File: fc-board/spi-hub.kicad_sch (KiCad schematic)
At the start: 22 parts, among them J15 BCS-110-L-D-TE, U10 LTC2983ILX-PBF

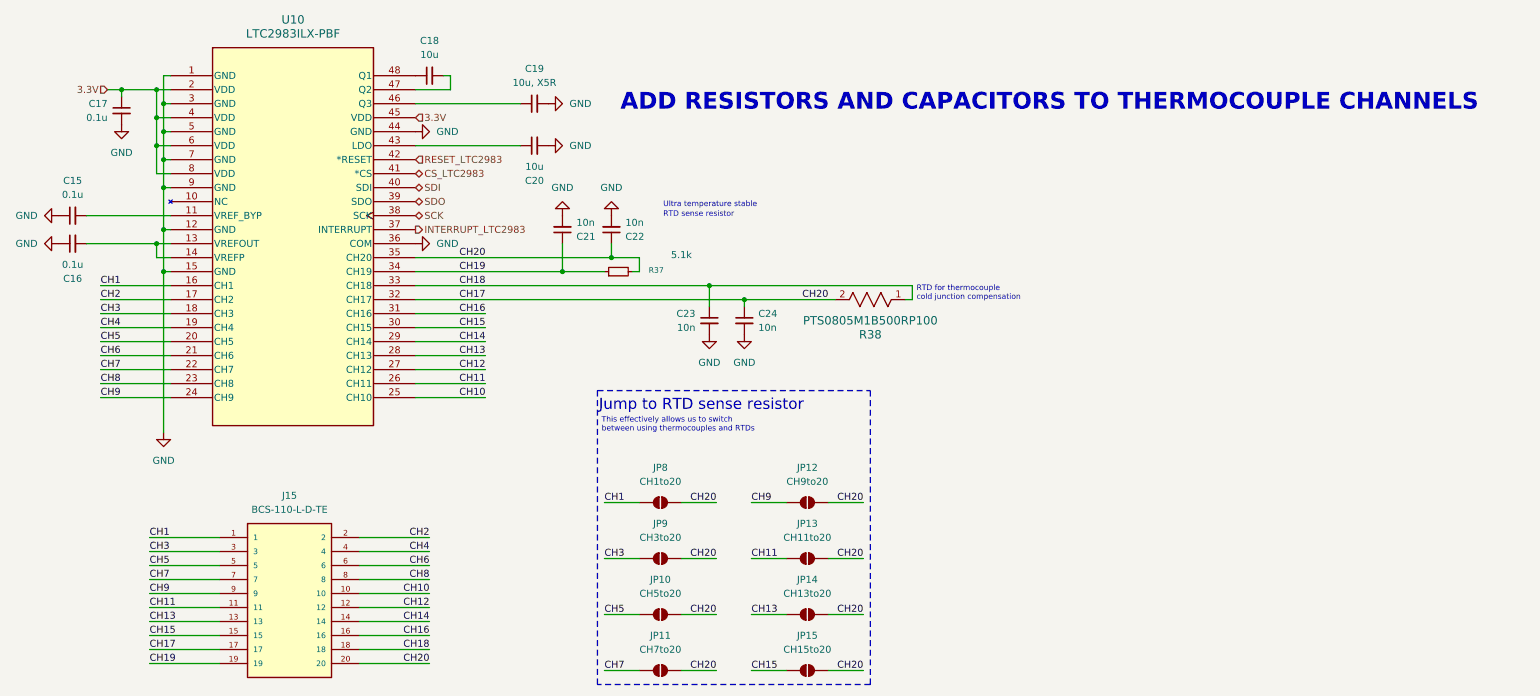
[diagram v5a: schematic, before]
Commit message: Fixed incorrect routes, modified gondola eth, cosmetics
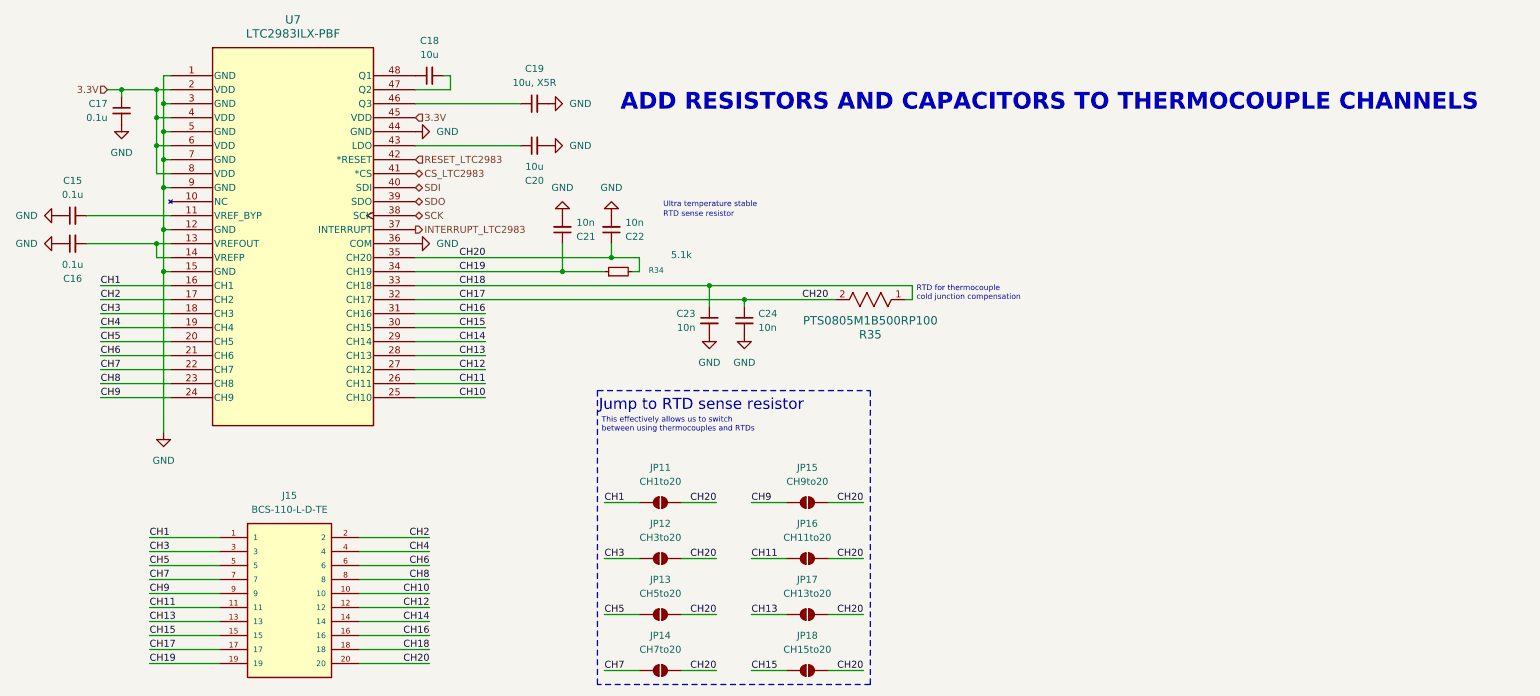
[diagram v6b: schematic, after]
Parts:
- renumbered JP8 to JP11, JP9 to JP12, JP10 to JP13, JP11 to JP14, JP12 to JP15, JP13 to JP16, JP14 to JP17, JP15 to JP18, R37 to R34, R38 to R35, U10 to U7
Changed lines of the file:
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@@
 	(title_block
 		(title "SPI Hub")
-		(date "2025-10-20")
+		(date "2025-12-08")
 		(rev "0.1")
 	)
@@
 		(dnp no)
 		(fields_autoplaced yes)
-		(property "Reference" "#PWR055"
+		(property "Reference" "#PWR052"
 			(at 43.18 100.33 0)
 			(effects
@@
 			(project "fc-board"
 				(path "/14bbabed-904f-4efc-8ba4-be00e59385c4/11d9cd03-29fa-40fa-a963-f5f11b91a482"
-					(reference "#PWR055")
+					(reference "#PWR052")
 					(unit 1)
 				)
@@
 		(dnp no)
 		(fields_autoplaced yes)
-		(property "Reference" "U10"
+		(property "Reference" "U7"
 			(at 66.675 19.05 0)
 			(effects
@@
 			(project ""
 				(path "/14bbabed-904f-4efc-8ba4-be00e59385c4/11d9cd03-29fa-40fa-a963-f5f11b91a482"
-					(reference "U10")
+					(reference "U7")
 					(unit 1)
 				)
@@
 		(dnp no)
 		(fields_autoplaced yes)
-		(property "Reference" "JP15"
+		(property "Reference" "JP18"
 			(at 160.02 130.81 0)
 			(effects
@@
 			(project ""
 				(path "/14bbabed-904f-4efc-8ba4-be00e59385c4/11d9cd03-29fa-40fa-a963-f5f11b91a482"
-					(reference "JP15")
+					(reference "JP18")
 					(unit 1)
 				)
@@
 		(dnp no)
 		(fields_autoplaced yes)
-		(property "Reference" "#PWR057"
+		(property "Reference" "#PWR054"
 			(at 95.25 59.69 0)
 			(effects
@@
 			(project "fc-board"
 				(path "/14bbabed-904f-4efc-8ba4-be00e59385c4/11d9cd03-29fa-40fa-a963-f5f11b91a482"
-					(reference "#PWR057")
+					(reference "#PWR054")
 					(unit 1)
 				)
@@
 		(dnp no)
 		(fields_autoplaced yes)
-		(property "Reference" "JP11"
+		(property "Reference" "JP14"
 			(at 133.35 130.81 0)
 			(effects
@@
 			(project "fc-board"
 				(path "/14bbabed-904f-4efc-8ba4-be00e59385c4/11d9cd03-29fa-40fa-a963-f5f11b91a482"
-					(reference "JP11")
+					(reference "JP14")
 					(unit 1)
 				)
@@
 		(dnp no)
 		(fields_autoplaced yes)
-		(property "Reference" "JP14"
+		(property "Reference" "JP17"
 			(at 160.02 120.65 0)
 			(effects
@@
 			(project "fc-board"
 				(path "/14bbabed-904f-4efc-8ba4-be00e59385c4/11d9cd03-29fa-40fa-a963-f5f11b91a482"
-					(reference "JP14")
+					(reference "JP17")
 					(unit 1)
 				)
@@
 		(on_board yes)
 		(dnp no)
-		(property "Reference" "R38"
+		(property "Reference" "R35"
 			(at 171.45 76.2 0)
 			(effects
@@
 			(project ""
 				(path "/14bbabed-904f-4efc-8ba4-be00e59385c4/11d9cd03-29fa-40fa-a963-f5f11b91a482"
-					(reference "R38")
+					(reference "R35")
 					(unit 1)
 				)
@@
 		(dnp no)
 		(fields_autoplaced yes)
-		(property "Reference" "JP13"
+		(property "Reference" "JP16"
 			(at 160.02 110.49 0)
 			(effects
@@
 			(project "fc-board"
 				(path "/14bbabed-904f-4efc-8ba4-be00e59385c4/11d9cd03-29fa-40fa-a963-f5f11b91a482"
-					(reference "JP13")
+					(reference "JP16")
 					(unit 1)
 				)
@@
 		(dnp no)
 		(fields_autoplaced yes)
-		(property "Reference" "JP9"
+		(property "Reference" "JP12"
 			(at 133.35 110.49 0)
 			(effects
@@
 			(project "fc-board"
 				(path "/14bbabed-904f-4efc-8ba4-be00e59385c4/11d9cd03-29fa-40fa-a963-f5f11b91a482"
-					(reference "JP9")
+					(reference "JP12")
 					(unit 1)
 				)
@@
 		(on_board yes)
 		(dnp no)
-		(property "Reference" "#PWR062"
+		(property "Reference" "#PWR059"
 			(at 142.24 82.55 0)
 			(effects
@@
 			(project "fc-board"
 				(path "/14bbabed-904f-4efc-8ba4-be00e59385c4/11d9cd03-29fa-40fa-a963-f5f11b91a482"
-					(reference "#PWR062")
+					(reference "#PWR059")
 					(unit 1)
 				)
@@
 		(dnp no)
 		(fields_autoplaced yes)
-		(property "Reference" "JP12"
+		(property "Reference" "JP15"
 			(at 160.02 100.33 0)
 			(effects
@@
 			(project "fc-board"
 				(path "/14bbabed-904f-4efc-8ba4-be00e59385c4/11d9cd03-29fa-40fa-a963-f5f11b91a482"
-					(reference "JP12")
+					(reference "JP15")
 					(unit 1)
 				)
@@
 		(dnp no)
 		(fields_autoplaced yes)
-		(property "Reference" "#PWR061"
+		(property "Reference" "#PWR058"
 			(at 124.46 48.26 0)
 			(effects
@@
 			(project "fc-board"
 				(path "/14bbabed-904f-4efc-8ba4-be00e59385c4/11d9cd03-29fa-40fa-a963-f5f11b91a482"
-					(reference "#PWR061")
+					(reference "#PWR058")
 					(unit 1)
 				)
@@
 		(dnp no)
 		(fields_autoplaced yes)
-		(property "Reference" "JP10"
+		(property "Reference" "JP13"
 			(at 133.35 120.65 0)
 			(effects
@@
 			(project "fc-board"
 				(path "/14bbabed-904f-4efc-8ba4-be00e59385c4/11d9cd03-29fa-40fa-a963-f5f11b91a482"
-					(reference "JP10")
+					(reference "JP13")
 					(unit 1)
 				)
@@
 		(dnp no)
 		(fields_autoplaced yes)
-		(property "Reference" "JP8"
+		(property "Reference" "JP11"
 			(at 133.35 100.33 0)
 			(effects
@@
 			(project "fc-board"
 				(path "/14bbabed-904f-4efc-8ba4-be00e59385c4/11d9cd03-29fa-40fa-a963-f5f11b91a482"
-					(reference "JP8")
+					(reference "JP11")
 					(unit 1)
 				)
@@
 		(on_board yes)
 		(dnp no)
-		(property "Reference" "#PWR063"
+		(property "Reference" "#PWR060"
 			(at 148.59 82.55 0)
 			(effects
@@
 			(project "fc-board"
 				(path "/14bbabed-904f-4efc-8ba4-be00e59385c4/11d9cd03-29fa-40fa-a963-f5f11b91a482"
-					(reference "#PWR063")
+					(reference "#PWR060")
 					(unit 1)
 				)
@@
 		(dnp no)
 		(fields_autoplaced yes)
-		(property "Reference" "#PWR054"
+		(property "Reference" "#PWR051"
 			(at 35.56 44.45 0)
 			(effects
@@
 			(project ""
 				(path "/14bbabed-904f-4efc-8ba4-be00e59385c4/11d9cd03-29fa-40fa-a963-f5f11b91a482"
-					(reference "#PWR054")
+					(reference "#PWR051")
 					(unit 1)
 				)
@@
 		(dnp no)
 		(fields_autoplaced yes)
-		(property "Reference" "#PWR056"
+		(property "Reference" "#PWR053"
 			(at 95.25 39.37 0)
 			(effects
@@
 			(project "fc-board"
 				(path "/14bbabed-904f-4efc-8ba4-be00e59385c4/11d9cd03-29fa-40fa-a963-f5f11b91a482"
-					(reference "#PWR056")
+					(reference "#PWR053")
 					(unit 1)
 				)
@@
 		(dnp no)
 		(fields_autoplaced yes)
-		(property "Reference" "#PWR052"
+		(property "Reference" "#PWR049"
 			(at 17.78 54.61 0)
 			(effects
@@
 			(project ""
 				(path "/14bbabed-904f-4efc-8ba4-be00e59385c4/11d9cd03-29fa-40fa-a963-f5f11b91a482"
-					(reference "#PWR052")
+					(reference "#PWR049")
 					(unit 1)
 				)
@@
 		(dnp no)
 		(fields_autoplaced yes)
-		(property "Reference" "#PWR058"
+		(property "Reference" "#PWR055"
 			(at 119.38 34.29 0)
 			(effects
@@
 			(project "fc-board"
 				(path "/14bbabed-904f-4efc-8ba4-be00e59385c4/11d9cd03-29fa-40fa-a963-f5f11b91a482"
-					(reference "#PWR058")
+					(reference "#PWR055")
 					(unit 1)
 				)
@@
 		(dnp no)
 		(fields_autoplaced yes)
-		(property "Reference" "#PWR053"
+		(property "Reference" "#PWR050"
 			(at 17.78 59.69 0)
 			(effects
@@
 			(project "fc-board"
 				(path "/14bbabed-904f-4efc-8ba4-be00e59385c4/11d9cd03-29fa-40fa-a963-f5f11b91a482"
-					(reference "#PWR053")
+					(reference "#PWR050")
 					(unit 1)
 				)
@@
 		(on_board yes)
 		(dnp no)
-		(property "Reference" "#PWR060"
+		(property "Reference" "#PWR057"
 			(at 115.57 48.26 0)
 			(effects
@@
 			(project "fc-board"
 				(path "/14bbabed-904f-4efc-8ba4-be00e59385c4/11d9cd03-29fa-40fa-a963-f5f11b91a482"
-					(reference "#PWR060")
+					(reference "#PWR057")
 					(unit 1)
 				)
@@
 		(dnp no)
 		(fields_autoplaced yes)
-		(property "Reference" "#PWR059"
+		(property "Reference" "#PWR056"
 			(at 119.38 41.91 0)
 			(effects
@@
 			(project "fc-board"
 				(path "/14bbabed-904f-4efc-8ba4-be00e59385c4/11d9cd03-29fa-40fa-a963-f5f11b91a482"
-					(reference "#PWR059")
+					(reference "#PWR056")
 					(unit 1)
 				)
@@
 		(on_board yes)
 		(dnp no)
-		(property "Reference" "R37"
+		(property "Reference" "R34"
 			(at 132.588 64.516 90)
 			(effects
@@
 			(project ""
 				(path "/14bbabed-904f-4efc-8ba4-be00e59385c4/11d9cd03-29fa-40fa-a963-f5f11b91a482"
-					(reference "R37")
+					(reference "R34")
 					(unit 1)
 				)

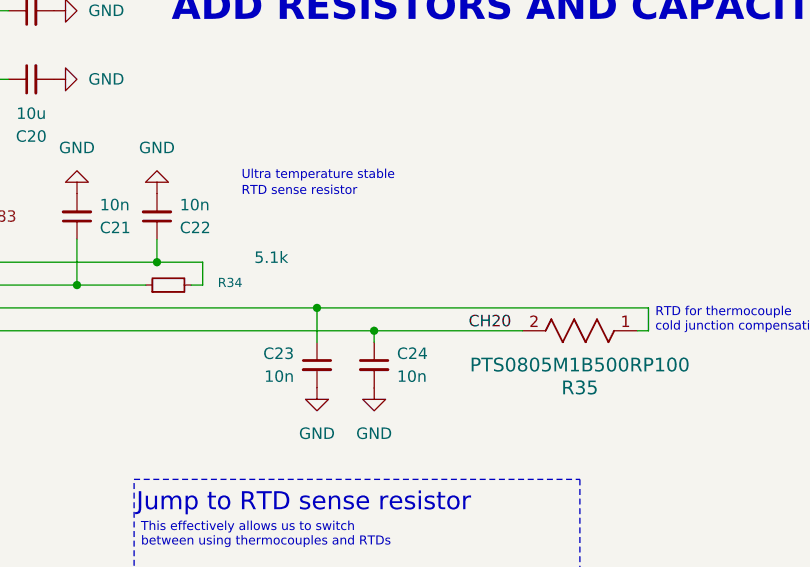
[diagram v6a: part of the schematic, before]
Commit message: Fixed PCIe routing, voltage sensing, added DAQ toggle, LCT interrupt, bias sensing resistors, SD card, and more
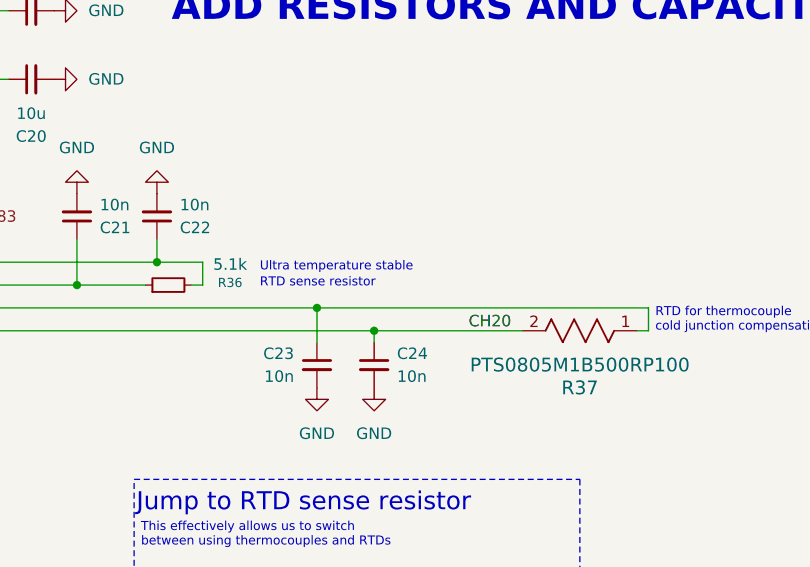
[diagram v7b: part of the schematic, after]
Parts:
- renumbered R34 to R36, R35 to R37
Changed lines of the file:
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@@
 	(text "Ultra temperature stable"
 		(exclude_from_sim no)
-		(at 133.858 52.07 0)
+		(at 135.89 62.23 0)
 		(effects
 			(font
@@
 	(text "RTD sense resistor"
 		(exclude_from_sim no)
-		(at 133.858 53.848 0)
+		(at 135.89 64.008 0)
 		(effects
 			(font
@@
 		(on_board yes)
 		(dnp no)
-		(property "Reference" "R35"
+		(property "Reference" "R37"
 			(at 171.45 76.2 0)
 			(effects
@@
 			(project ""
 				(path "/14bbabed-904f-4efc-8ba4-be00e59385c4/11d9cd03-29fa-40fa-a963-f5f11b91a482"
-					(reference "R35")
+					(reference "R37")
 					(unit 1)
 				)
@@
 		(on_board yes)
 		(dnp no)
-		(property "Reference" "R34"
+		(property "Reference" "R36"
 			(at 132.588 64.516 90)
 			(effects
@@
 		)
 		(property "Value" "5.1k"
-			(at 137.16 61.722 90)
+			(at 132.588 62.484 90)
 			(effects
 				(font
@@
 			(project ""
 				(path "/14bbabed-904f-4efc-8ba4-be00e59385c4/11d9cd03-29fa-40fa-a963-f5f11b91a482"
-					(reference "R34")
+					(reference "R36")
 					(unit 1)
 				)
